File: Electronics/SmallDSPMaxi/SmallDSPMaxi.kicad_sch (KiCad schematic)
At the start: 99 parts, among them J1 Header, J10 Header, J11 Programming, J2 Header, J3 Header, J4 Header, J5 Header, J6 Header, J7 Header, J8 Header, J9 Header, Q1 NSS1C300ET4G, SW1 SW_4PDT, SW2 TS-1187A-B-A-B, U1 ADAU1467, U2 ADM811, U3 M95M01-R, Y1 830105957509

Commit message: Fixes minor issues
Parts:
- removed R28: 100k, Resistor_SMD:R_0402_1005Metric, symbol Device:R_Small
- added R90: 10k, Resistor_SMD:R_0402_1005Metric, symbol Device:R_Small
- R3: value 4k3 -> 10k; footprint Resistor_SMD:R_0603_1608Metric -> Resistor_SMD:R_0402_1005Metric; LCSC Part # C23159 -> C25744; Part Number 0603WAF4301T5E -> 0402WGF1002TCE; Rated Power 100mW -> 62.5mW
- R32: value 100k -> 10k; LCSC Part # C25741 -> C25744; Part Number 0402WGF1003TCE -> 0402WGF1002TCE
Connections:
- net +3V3: now also R32.1, R90.1; no longer R32.2
- net ~{CS EEPROM}: now also R90.2
- net ~{DSP RST}: now also R32.2; no longer R32.1
- no-connect marks 17 -> 18
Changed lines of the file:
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@@
   (title_block
     (title "SmallDSP Maxi")
-    (date "2023-11-02")
+    (date "2023-11-05")
     (rev "1.0")
     (company "Till Heuer")
@@
   (no_connect (at 101.6 154.94))
   (no_connect (at 101.6 147.32))
+  (no_connect (at 25.4 175.26))
   (no_connect (at 101.6 152.4))
   (no_connect (at 220.98 137.16))
@@
     )
   )
-  (symbol (lib_id "Device:R_Small") (at 166.37 175.26 180) (unit 1)
-    (in_bom yes) (on_board yes) (dnp yes) (fields_autoplaced)
-    (property "Reference" "R28" (at 167.8686 174.0479 0)
-      (effects (font (size 1.27 1.27)) (justify right))
-    )
-    (property "Value" "100k" (at 167.8686 176.4721 0)
-      (effects (font (size 1.27 1.27)) (justify right))
-    )
-    (property "Footprint" "Resistor_SMD:R_0402_1005Metric" (at 166.37 175.26 0)
-      (effects (font (size 1.27 1.27)) hide)
-    )
-    (property "Datasheet" "~" (at 166.37 175.26 0)
-      (effects (font (size 1.27 1.27)) hide)
-    )
-    (property "Dielectric" "" (at 166.37 175.26 0)
-      (effects (font (size 1.27 1.27)) hide)
-    )
-    (property "Notes" "" (at 166.37 175.26 0)
-      (effects (font (size 1.27 1.27)) hide)
-    )
-    (property "Rated Voltage" "" (at 166.37 175.26 0)
-      (effects (font (size 1.27 1.27)) hide)
-    )
-    (property "Assembling" "X" (at 166.37 175.26 0)
-      (effects (font (size 1.27 1.27)) hide)
-    )
-    (property "Manufacturer" "UNI-ROYAL(Uniroyal Elec)" (at 166.37 175.26 0)
-      (effects (font (size 1.27 1.27)) hide)
-    )
-    (property "Rated Power" "62.5mW" (at 166.37 175.26 0)
-      (effects (font (size 1.27 1.27)) hide)
-    )
-    (property "Part Number" "0402WGF1003TCE" (at 166.37 175.26 0)
-      (effects (font (size 1.27 1.27)) hide)
-    )
-    (property "Rated Current" "" (at 166.37 175.26 0)
-      (effects (font (size 1.27 1.27)) hide)
-    )
-    (property "Tolerance" "1%" (at 166.37 175.26 0)
-      (effects (font (size 1.27 1.27)) hide)
-    )
-    (property "LCSC Part #" "C25741" (at 166.37 175.26 0)
-      (effects (font (size 1.27 1.27)) hide)
-    )
-    (pin "1")
-    (pin "2")
-    (instances
-      (project "SmallDSPMaxi"
-        (path "/5f2729b5-edcd-4fbc-b3fb-44096724c941"
-          (reference "R28") (unit 1)
-        )
-      )
-    )
-  )
   (symbol (lib_id "Connector:TestPoint") (at 38.1 20.32 0) (unit 1)
     (in_bom yes) (on_board yes) (dnp yes) (fields_autoplaced)
@@
     )
   )
+  (symbol (lib_id "Device:R_Small") (at 166.37 175.26 0) (unit 1)
+    (in_bom yes) (on_board yes) (dnp no) (fields_autoplaced)
+    (property "Reference" "R90" (at 167.8686 174.0479 0)
+      (effects (font (size 1.27 1.27)) (justify left))
+    )
+    (property "Value" "10k" (at 167.8686 176.4721 0)
+      (effects (font (size 1.27 1.27)) (justify left))
+    )
+    (property "Footprint" "Resistor_SMD:R_0402_1005Metric" (at 166.37 175.26 0)
+      (effects (font (size 1.27 1.27)) hide)
+    )
+    (property "Datasheet" "~" (at 166.37 175.26 0)
+      (effects (font (size 1.27 1.27)) hide)
+    )
+    (property "Dielectric" "" (at 166.37 175.26 0)
+      (effects (font (size 1.27 1.27)) hide)
+    )
+    (property "Notes" "" (at 166.37 175.26 0)
+      (effects (font (size 1.27 1.27)) hide)
+    )
+    (property "Rated Voltage" "" (at 166.37 175.26 0)
+      (effects (font (size 1.27 1.27)) hide)
+    )
+    (property "Assembling" "X" (at 166.37 175.26 0)
+      (effects (font (size 1.27 1.27)) hide)
+    )
+    (property "Manufacturer" "UNI-ROYAL(Uniroyal Elec)" (at 166.37 175.26 0)
+      (effects (font (size 1.27 1.27)) hide)
+    )
+    (property "Rated Power" "62.5mW" (at 166.37 175.26 0)
+      (effects (font (size 1.27 1.27)) hide)
+    )
+    (property "Part Number" "0402WGF1002TCE" (at 166.37 175.26 0)
+      (effects (font (size 1.27 1.27)) hide)
+    )
+    (property "Rated Current" "" (at 166.37 175.26 0)
+      (effects (font (size 1.27 1.27)) hide)
+    )
+    (property "Tolerance" "1%" (at 166.37 175.26 0)
+      (effects (font (size 1.27 1.27)) hide)
+    )
+    (property "LCSC Part #" "C25744" (at 166.37 175.26 0)
+      (effects (font (size 1.27 1.27)) hide)
+    )
+    (pin "1")
+    (pin "2")
+    (instances
+      (project "SmallDSPMaxi"
+        (path "/5f2729b5-edcd-4fbc-b3fb-44096724c941"
+          (reference "R90") (unit 1)
+        )
+      )
+    )
+  )
   (symbol (lib_name "ADAU1463_1") (lib_id "1_Project_Symbols:ADAU1463") (at 128.27 95.25 0) (unit 3)
     (in_bom yes) (on_board yes) (dnp no)
@@
     )
   )
-  (symbol (lib_id "Device:R_Small") (at 214.63 121.92 180) (unit 1)
-    (in_bom yes) (on_board yes) (dnp yes) (fields_autoplaced)
-    (property "Reference" "R32" (at 216.1286 120.7079 0)
-      (effects (font (size 1.27 1.27)) (justify right))
-    )
-    (property "Value" "100k" (at 216.1286 123.1321 0)
-      (effects (font (size 1.27 1.27)) (justify right))
-    )
-    (property "Footprint" "Resistor_SMD:R_0402_1005Metric" (at 214.63 121.92 0)
-      (effects (font (size 1.27 1.27)) hide)
-    )
-    (property "Datasheet" "~" (at 214.63 121.92 0)
-      (effects (font (size 1.27 1.27)) hide)
-    )
-    (property "Dielectric" "" (at 214.63 121.92 0)
-      (effects (font (size 1.27 1.27)) hide)
-    )
-    (property "Notes" "" (at 214.63 121.92 0)
-      (effects (font (size 1.27 1.27)) hide)
-    )
-    (property "Rated Voltage" "" (at 214.63 121.92 0)
-      (effects (font (size 1.27 1.27)) hide)
-    )
-    (property "Assembling" "X" (at 214.63 121.92 0)
-      (effects (font (size 1.27 1.27)) hide)
-    )
-    (property "Manufacturer" "UNI-ROYAL(Uniroyal Elec)" (at 214.63 121.92 0)
-      (effects (font (size 1.27 1.27)) hide)
-    )
-    (property "Rated Power" "62.5mW" (at 214.63 121.92 0)
-      (effects (font (size 1.27 1.27)) hide)
-    )
-    (property "Part Number" "0402WGF1003TCE" (at 214.63 121.92 0)
-      (effects (font (size 1.27 1.27)) hide)
-    )
-    (property "Rated Current" "" (at 214.63 121.92 0)
-      (effects (font (size 1.27 1.27)) hide)
-    )
-    (property "Tolerance" "1%" (at 214.63 121.92 0)
-      (effects (font (size 1.27 1.27)) hide)
-    )
-    (property "LCSC Part #" "C25741" (at 214.63 121.92 0)
-      (effects (font (size 1.27 1.27)) hide)
-    )
-    (pin "1")
-    (pin "2")
-    (instances
-      (project "SmallDSPMaxi"
-        (path "/5f2729b5-edcd-4fbc-b3fb-44096724c941"
-          (reference "R32") (unit 1)
-        )
-      )
-    )
-  )
   (symbol (lib_id "power:+3V3") (at 214.63 118.11 0) (unit 1)
     (in_bom yes) (on_board yes) (dnp no)
@@
     )
   )
+  (symbol (lib_id "Device:R_Small") (at 214.63 121.92 0) (unit 1)
+    (in_bom yes) (on_board yes) (dnp yes) (fields_autoplaced)
+    (property "Reference" "R32" (at 216.1286 120.7079 0)
+      (effects (font (size 1.27 1.27)) (justify left))
+    )
+    (property "Value" "10k" (at 216.1286 123.1321 0)
+      (effects (font (size 1.27 1.27)) (justify left))
+    )
+    (property "Footprint" "Resistor_SMD:R_0402_1005Metric" (at 214.63 121.92 0)
+      (effects (font (size 1.27 1.27)) hide)
+    )
+    (property "Datasheet" "~" (at 214.63 121.92 0)
+      (effects (font (size 1.27 1.27)) hide)
+    )
+    (property "Dielectric" "" (at 214.63 121.92 0)
+      (effects (font (size 1.27 1.27)) hide)
+    )
+    (property "Notes" "" (at 214.63 121.92 0)
+      (effects (font (size 1.27 1.27)) hide)
+    )
+    (property "Rated Voltage" "" (at 214.63 121.92 0)
+      (effects (font (size 1.27 1.27)) hide)
+    )
+    (property "Assembling" "X" (at 214.63 121.92 0)
+      (effects (font (size 1.27 1.27)) hide)
+    )
+    (property "Manufacturer" "UNI-ROYAL(Uniroyal Elec)" (at 214.63 121.92 0)
+      (effects (font (size 1.27 1.27)) hide)
+    )
+    (property "Rated Power" "62.5mW" (at 214.63 121.92 0)
+      (effects (font (size 1.27 1.27)) hide)
+    )
+    (property "Part Number" "0402WGF1002TCE" (at 214.63 121.92 0)
+      (effects (font (size 1.27 1.27)) hide)
+    )
+    (property "Rated Current" "" (at 214.63 121.92 0)
+      (effects (font (size 1.27 1.27)) hide)
+    )
+    (property "Tolerance" "1%" (at 214.63 121.92 0)
+      (effects (font (size 1.27 1.27)) hide)
+    )
+    (property "LCSC Part #" "C25744" (at 214.63 121.92 0)
+      (effects (font (size 1.27 1.27)) hide)
+    )
+    (pin "1")
+    (pin "2")
+    (instances
+      (project "SmallDSPMaxi"
+        (path "/5f2729b5-edcd-4fbc-b3fb-44096724c941"
+          (reference "R32") (unit 1)
+        )
+      )
+    )
+  )
   (symbol (lib_id "power:GND") (at 255.27 29.21 0) (unit 1)
     (in_bom yes) (on_board yes) (dnp no)
@@
       (effects (font (size 1.27 1.27)) (justify left))
     )
-    (property "Value" "4k3" (at 90.3986 163.7721 0)
+    (property "Value" "10k" (at 90.3986 163.7721 0)
       (effects (font (size 1.27 1.27)) (justify left))
     )
-    (property "Footprint" "Resistor_SMD:R_0603_1608Metric" (at 88.9 162.56 0)
+    (property "Footprint" "Resistor_SMD:R_0402_1005Metric" (at 88.9 162.56 0)
       (effects (font (size 1.27 1.27)) hide)
     )
@@
       (effects (font (size 1.27 1.27)) hide)
     )
-    (property "Rated Power" "100mW" (at 88.9 162.56 0)
+    (property "Rated Power" "62.5mW" (at 88.9 162.56 0)
       (effects (font (size 1.27 1.27)) hide)
     )
-    (property "Part Number" "0603WAF4301T5E" (at 88.9 162.56 0)
+    (property "Part Number" "0402WGF1002TCE" (at 88.9 162.56 0)
       (effects (font (size 1.27 1.27)) hide)
     )
@@
       (effects (font (size 1.27 1.27)) hide)
     )
-    (property "LCSC Part #" "C23159" (at 88.9 162.56 0)
+    (property "LCSC Part #" "C25744" (at 88.9 162.56 0)
       (effects (font (size 1.27 1.27)) hide)
     )

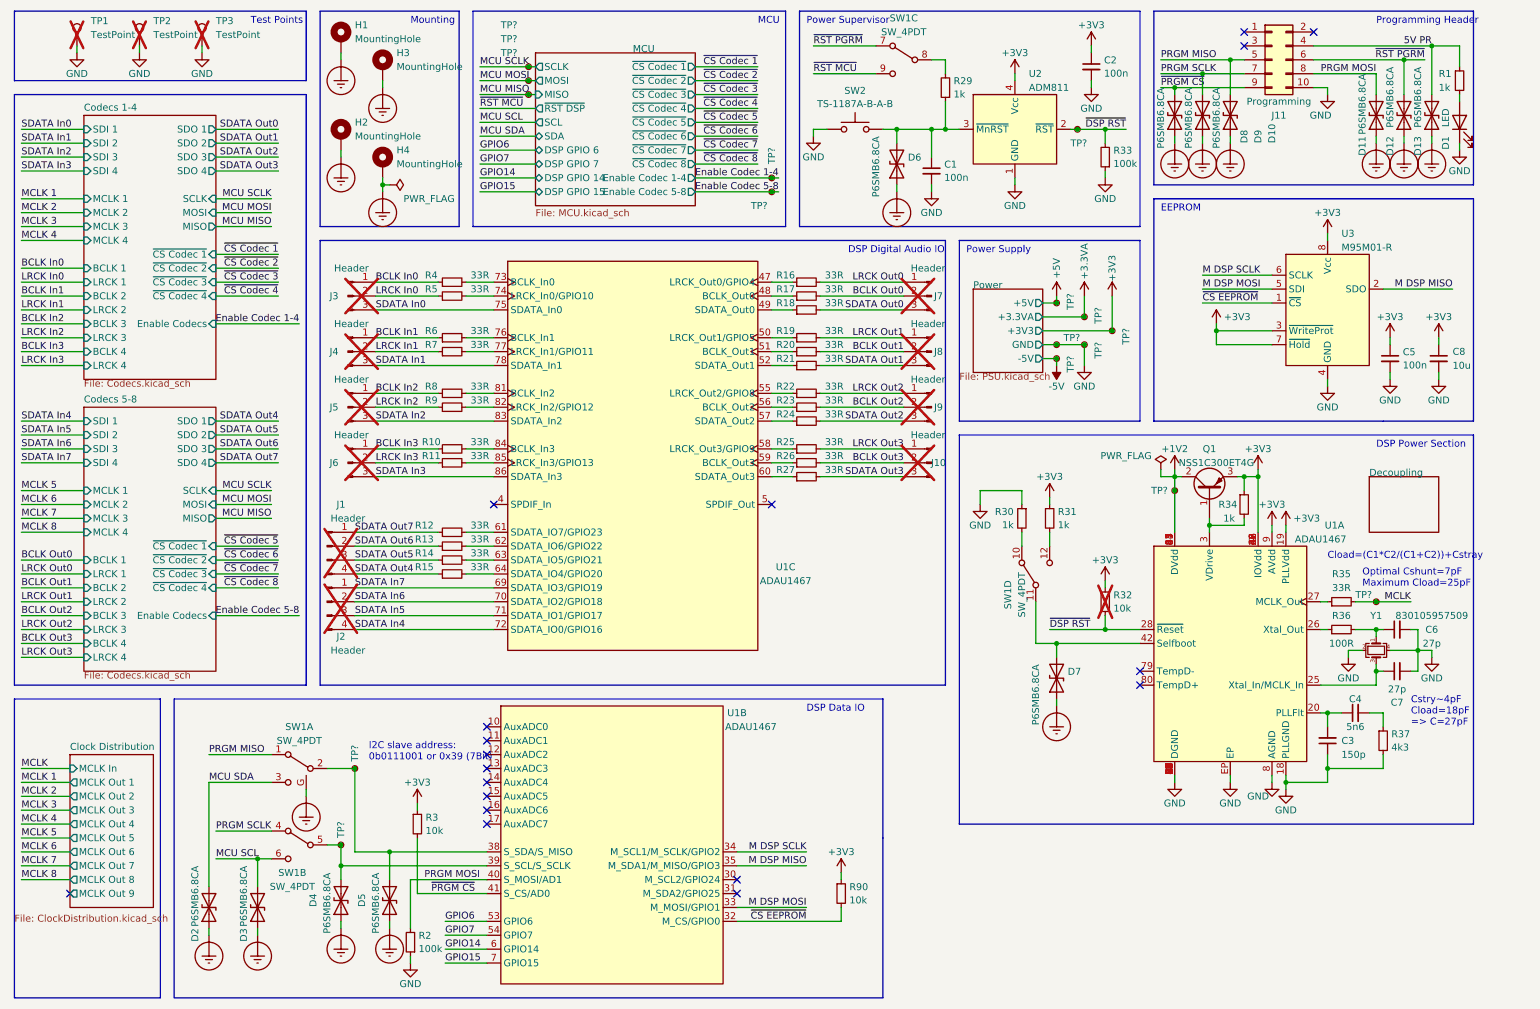
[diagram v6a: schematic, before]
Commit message: adds usb to i2s bridge to micro. Adds tweaks for layout of maxi.
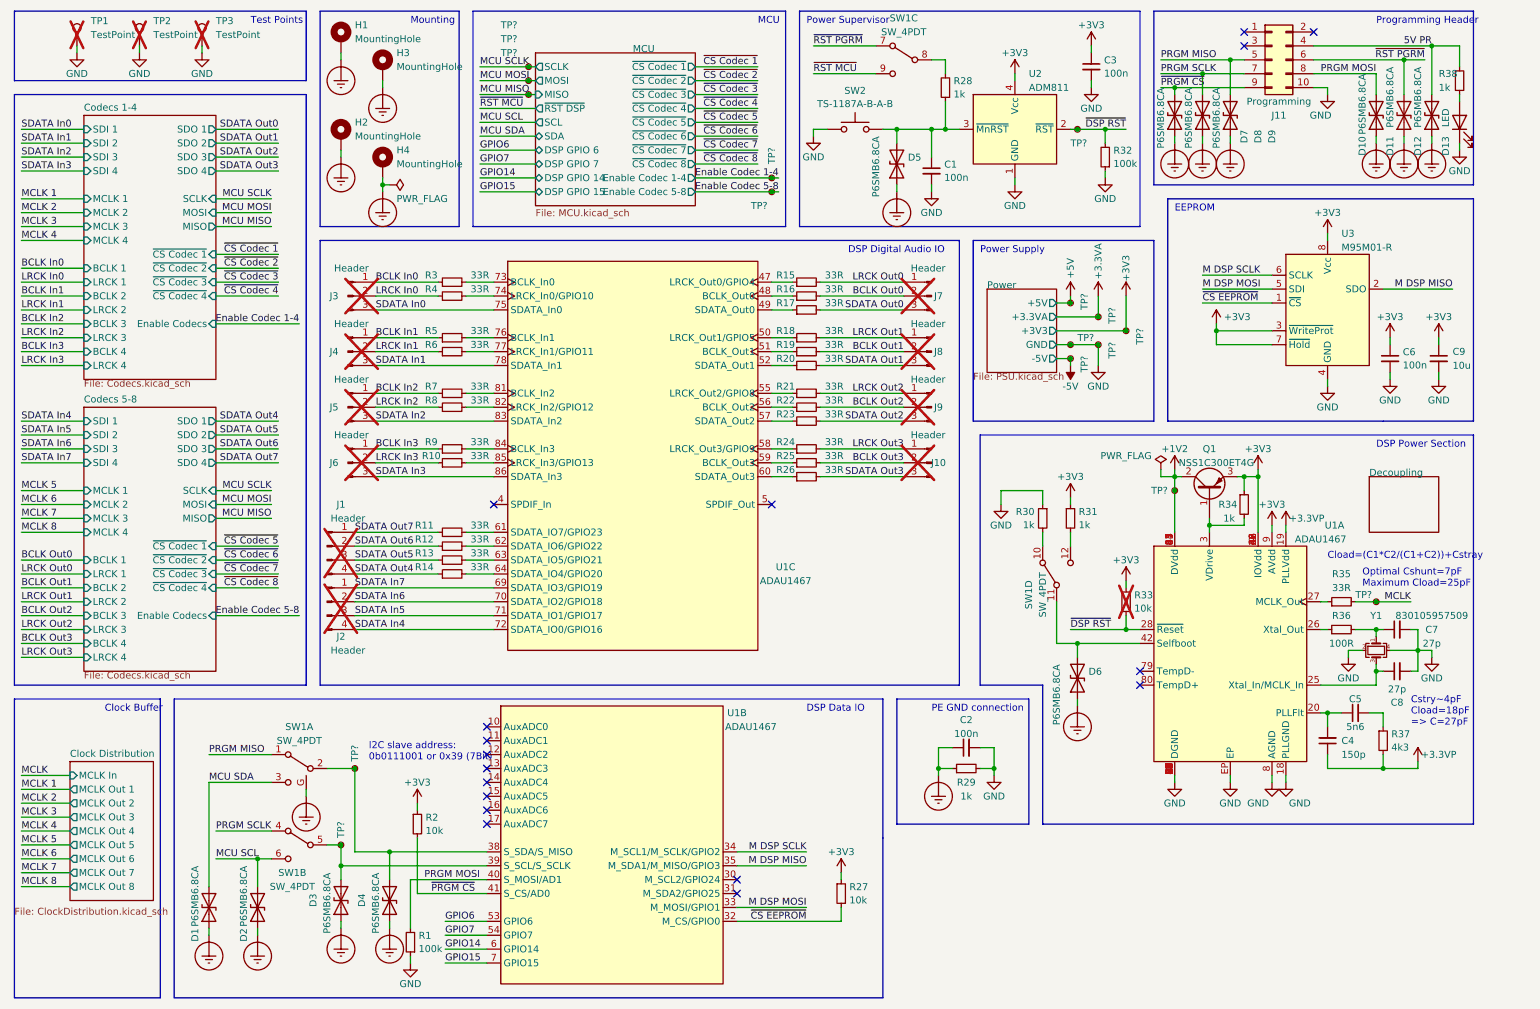
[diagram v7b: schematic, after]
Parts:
- added C2: 100n, Capacitor_SMD:C_0402_1005Metric, symbol Device:C_Small
- added R29: 1k, Resistor_SMD:R_0402_1005Metric, symbol Device:R_Small
- Q1: footprint Package_TO_SOT_SMD:TO-252-2 -> 1_Project_Footprints:TO-252-2 thermal vias
- renumbered C2 to C3, C3 to C4, C4 to C5, C5 to C6, C6 to C7, C7 to C8, C8 to C9, D2 to D1, D11 to D10, D12 to D11, D13 to D12, D1 to D13, D3 to D2, D4 to D3, D5 to D4, D6 to D5, D7 to D6, D8 to D7, D9 to D8, D10 to D9, R2 to R1, R11 to R10, R12 to R11, R13 to R12, R14 to R13, R15 to R14, R16 to R15, R17 to R16, R18 to R17, R19 to R18, R20 to R19, R3 to R2, R21 to R20, R22 to R21, R23 to R22, R24 to R23, R25 to R24, R26 to R25, R27 to R26, R90 to R27, R29 to R28, R4 to R3, R33 to R32, R32 to R33, R1 to R38, R5 to R4, R6 to R5, R7 to R6, R8 to R7, R9 to R8, R10 to R9
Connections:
- net +3V3: no longer U1.19 (PLLVdd)
- net Earth_Protective: now also C2.1, R29.1
- net GND: now also C2.2, R29.2; no longer C4.1, R37.2
- new net +3.3VP: C4.1, R37.2, U1.19 (PLLVdd)
- no-connect marks 18 -> 17
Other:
- sheet Clock Distribution ports: added none; removed MCLK Out 9
- note added: "Clock Buffer"
- note added: "PE GND connection"
- moved on the sheet: D6, R30, R31, R33, SW1D, TP?

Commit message: Fixes wrong connection in maxi schematic
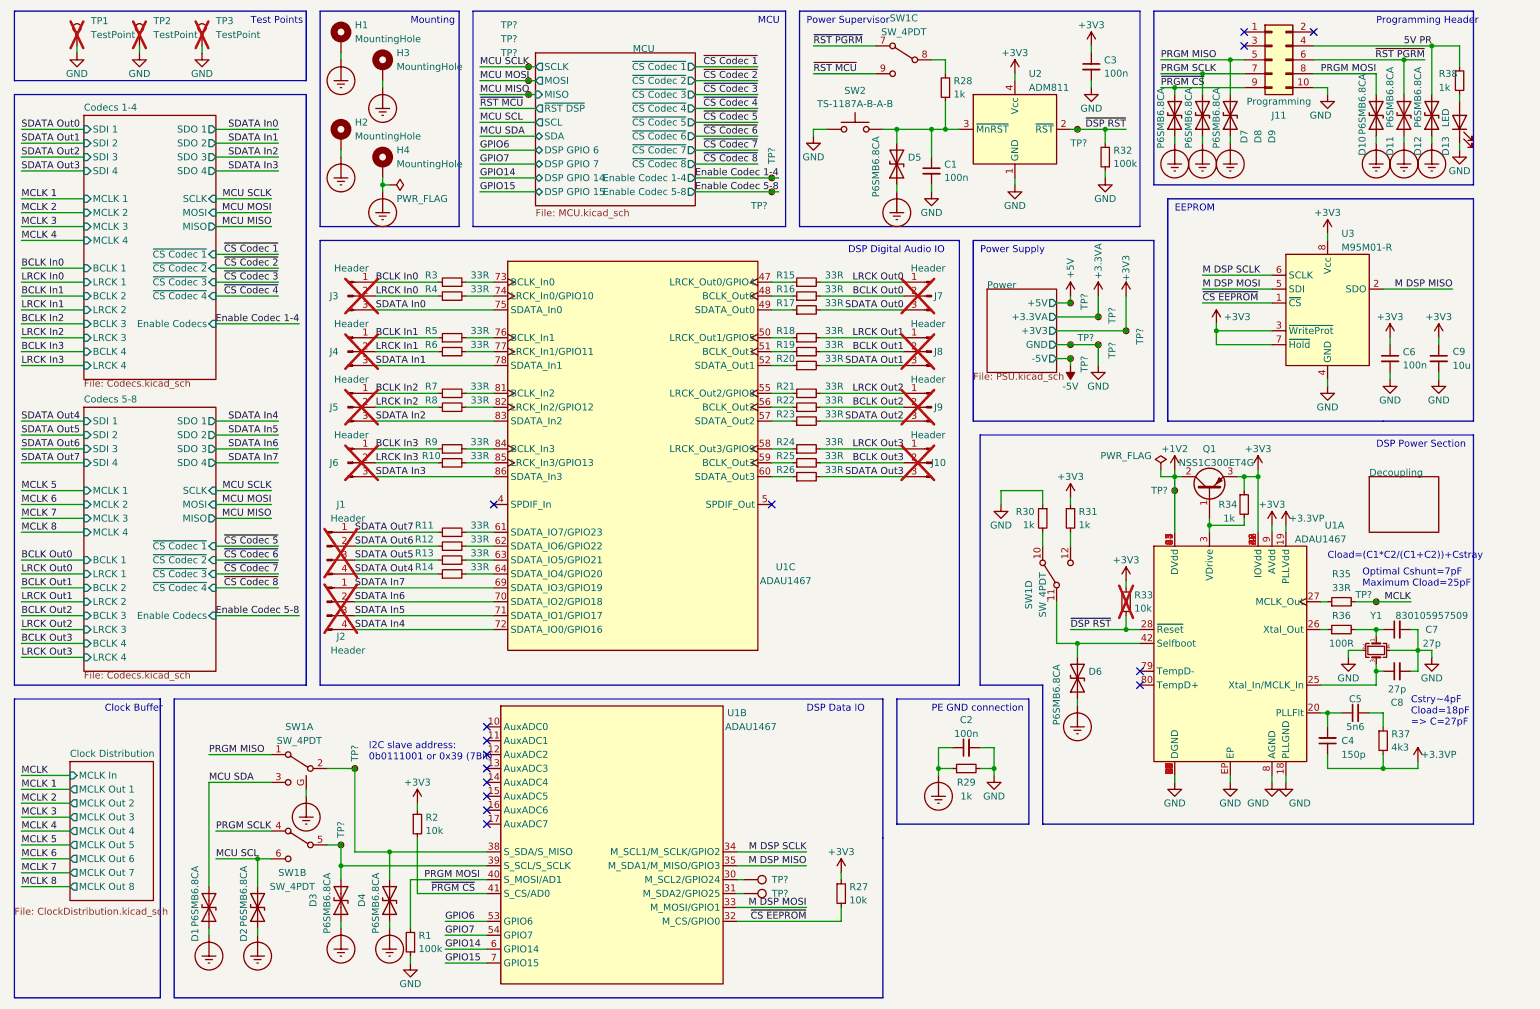
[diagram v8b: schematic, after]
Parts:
- added TP? (x2): TestPoint, TestPoint:TestPoint_Pad_D1.0mm, symbol Connector:TestPoint
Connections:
- net at U1.30 (M_SCL2/GPIO24): now also TP?.1
- net at U1.31 (M_SDA2/GPIO25): now also TP?.1
- no-connect marks 17 -> 15
